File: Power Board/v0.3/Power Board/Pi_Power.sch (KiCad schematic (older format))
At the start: 23 parts, among them Q1 SI5504BDC

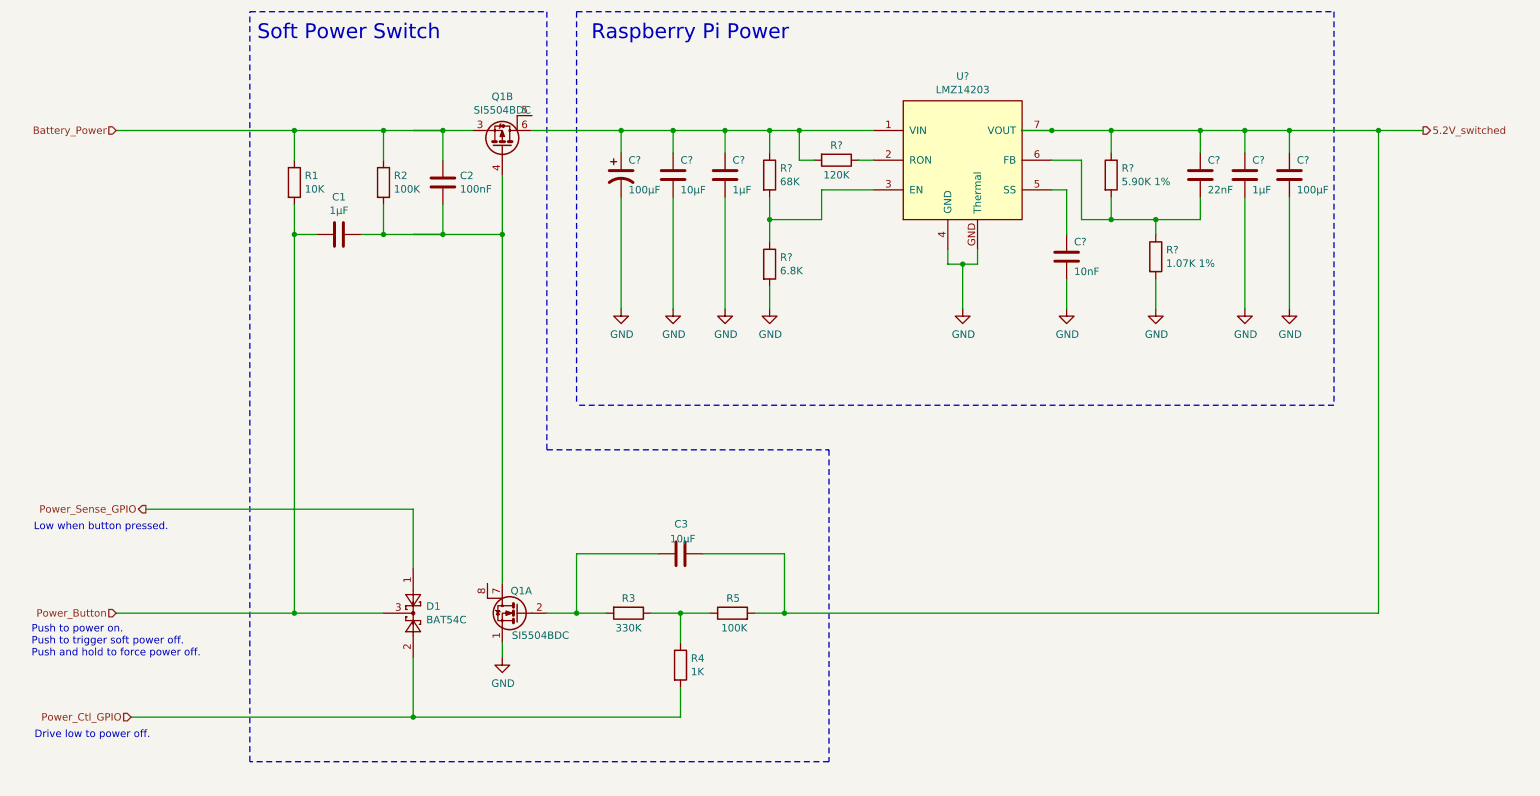
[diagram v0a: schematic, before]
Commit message: Create the LED panel supply circuit.
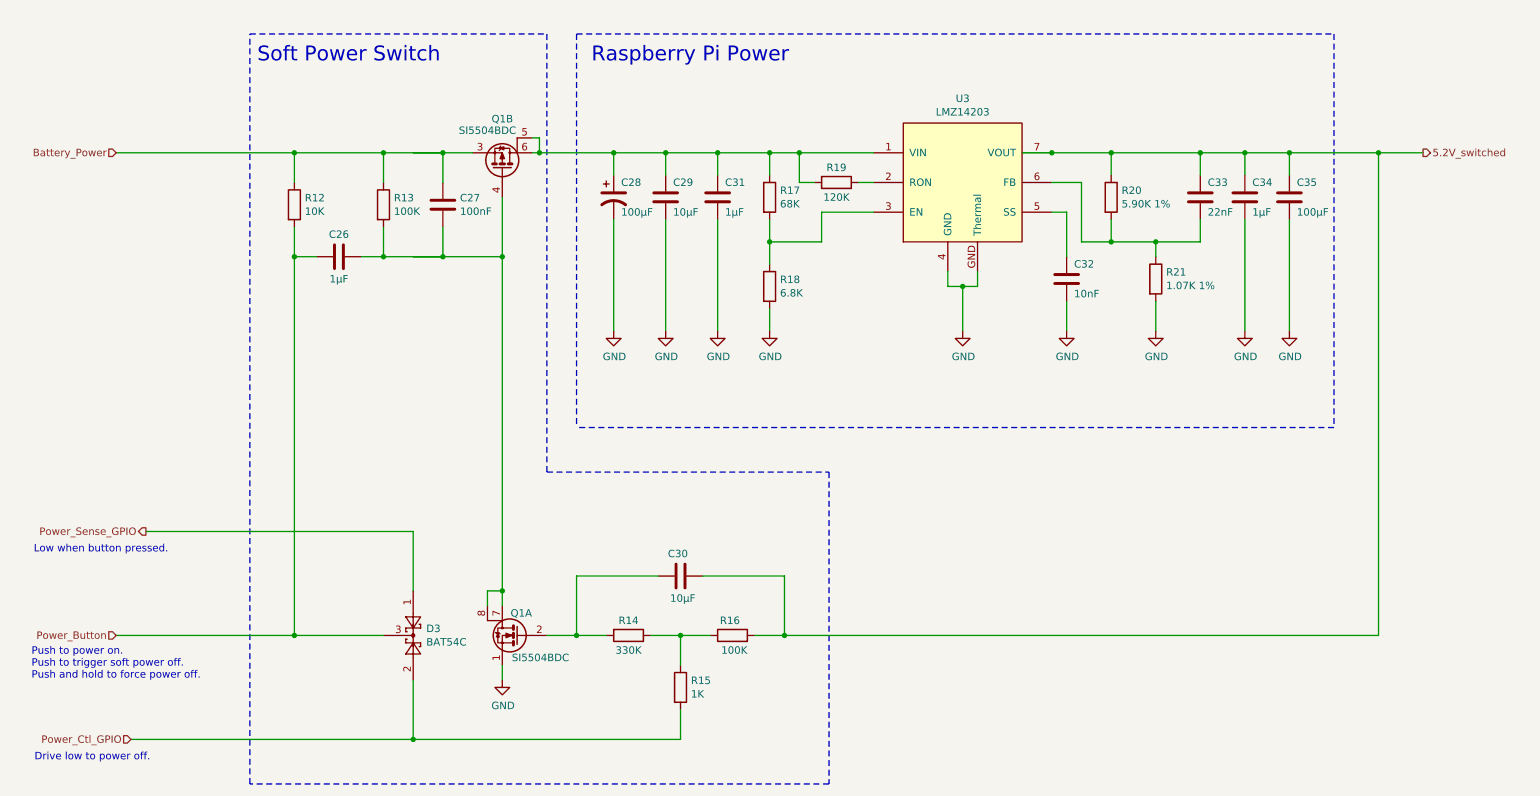
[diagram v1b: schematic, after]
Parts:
- gave numbers to parts that had none: 13
- renumbered C1 to C26, C2 to C27, C3 to C30, D1 to D3, R1 to R12, R2 to R13, R3 to R14, R4 to R15, R5 to R16
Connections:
- wire segments 92 -> 98
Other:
- moved on the sheet: C26, C27, C28, C29, C30, C31, C32, C33, C34, C35, D3, Q1A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

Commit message: Update components with available parts.
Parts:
- C1: renamed from C26; Digikey No. not avail. -> 587-1438-1-ND; Manufacturer NIC -> Taiyo Yuden; Part No. NMC0805X7R105K25TRPLPF -> GMK212B7105KG-T
- C10: renamed from C35; Digikey No. 587-5426-1-ND -> 587-1965-1-ND; Part No. EMK325ABJ107MM-P -> LMK325BJ107MM-T
- C2: renamed from C27; footprint Capacitor_SMD:C_0603_1608Metric -> Capacitor_SMD:C_0805_2012Metric; Digikey No. (none) -> 445-5827-1-ND; Manufacturer Murata -> TDK; Part No. GRM188R71C104KA01D -> CGA4J2X7R2A104K125AA
- C4: renamed from C29; footprint Capacitor_SMD:C_1210_3225Metric -> Capacitor_SMD:C_0805_2012Metric; Digikey No. (none) -> 490-10748-1-ND; Manufacturer (none) -> Murata; Part No. (none) -> GRM21BR61E106MA73L
- C5: renamed from C30; footprint Capacitor_SMD:C_1210_3225Metric -> Capacitor_SMD:C_0805_2012Metric; Digikey No. (none) -> 490-10748-1-ND; Manufacturer (none) -> Murata; Part No. (none) -> GRM21BR61E106MA73L
- C6: renamed from C31; Digikey No. not avail. -> 587-1438-1-ND; Manufacturer NIC -> Taiyo Yuden; Part No. NMC0805X7R105K25TRPLPF -> GMK212B7105KG-T
- C7: renamed from C32; Digikey No. (none) -> -; Manufacturer (none) -> Murata; Part No. (none) -> GRM188R71H103KA01D
- C8: renamed from C33; Digikey No. 490-1517-2-ND -> 732-8009-1-ND; Manufacturer Murata -> Wurth; Part No. GRM188R71H223KA01D -> 885012206091
- C9: renamed from C34; Digikey No. not avail. -> 587-1438-1-ND; Manufacturer NIC -> Taiyo Yuden; Part No. NMC0805X7R105K25TRPLPF -> GMK212B7105KG-T
- R10: renamed from R19; Digikey No. (none) -> -
- R3: renamed from R12; Digikey No. (none) -> -
- R4: renamed from R13; Digikey No. (none) -> -
- R5: renamed from R14; Digikey No. (none) -> -
- R6: renamed from R15; Digikey No. (none) -> -
- R7: renamed from R16; Digikey No. (none) -> -
- R8: renamed from R17; Digikey No. (none) -> -
- R9: renamed from R18; Digikey No. (none) -> -
- U1: renamed from U3; Digikey No. (none) -> -
- renumbered C28 to C3, R20 to R11, R21 to R12
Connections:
- wire segments 98 -> 97

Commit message: Draw all custom footprints and assign to components.
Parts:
- C3: footprint (none) -> Capacitor_SMD:CP_Elec_8x10
- Q1: footprint (none) -> Power_Board:1206-8_or_SO-8
- U1: footprint (none) -> Power_Board:TO-PMOD_7
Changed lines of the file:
@@
 F 0 "U1" H 7150 2915 50  0000 C CNN
 F 1 "LMZ14203" H 7150 2824 50  0000 C CNN
-F 2 "" H 7150 2350 50  0001 C CNN
+F 2 "Power_Board:TO-PMOD_7" H 7150 2350 50  0001 C CNN
 F 3 "" H 7150 2350 50  0001 C CNN
 F 4 "TI" H 850 250 50  0001 C CNN "Manufacturer"
@@
 F 0 "C3" H 4850 2550 50  0000 L CNN
 F 1 "100µF" H 4850 2350 50  0000 L CNN
-F 2 "" H 4800 2450 50  0001 C CNN
-F 3 "~" H 4800 2450 50  0001 C CNN
+F 2 "Capacitor_SMD:CP_Elec_8x10" H 4800 2450 50  0001 C CNN
+F 3 "https://datasheet.octopart.com/EDK107M050A9MAA-Kemet-datasheet-13271990.pdf" H 4800 2450 50  0001 C CNN
 F 4 "399-6672-1-ND" H 1200 -1250 50  0001 C CNN "Digikey No."
 F 5 "Kemet" H 1200 -1250 50  0001 C CNN "Manufacturer"
@@
 F 0 "Q1" V 4278 2150 50  0000 C CNN
 F 1 "SI5504BDC" V 4200 2050 50  0000 C CNN
-F 2 "" H 4050 2150 50  0001 C CNN
+F 2 "Power_Board:1206-8_or_SO-8" H 4050 2150 50  0001 C CNN
 F 3 "http://www.vishay.com/docs/74483/si5504bdc.pdf" H 4050 2150 50  0001 C CNN
 F 4 "SI5504BDC-T1-GE3CT-ND" H -1900 -800 50  0001 C CNN "Digikey No."
@@
 F 0 "Q1" H 3850 5550 50  0000 L CNN
 F 1 "SI5504BDC" H 3600 5250 50  0000 L CNN
-F 2 "" H 4050 5400 50  0001 C CNN
+F 2 "Power_Board:1206-8_or_SO-8" H 4050 5400 50  0001 C CNN
 F 3 "http://www.vishay.com/docs/74483/si5504bdc.pdf" H 4050 5400 50  0001 C CNN
 F 4 "SI5504BDC-T1-GE3CT-ND" H -1700 1350 50  0001 C CNN "Digikey No."

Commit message: Work in progress.
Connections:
- net Vin_switched: now reaches C3.1, C4.1, C6.1, Q1.5 (D), Q1.6 (D), R10.2, R8.1, U1.1 (VIN)
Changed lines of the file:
@@
 Connection ~ 3650 2850
 Connection ~ 3250 2850
+Text Label 4600 2150 0    50   ~ 0
+Vin_switched
 $EndSCHEMATC
